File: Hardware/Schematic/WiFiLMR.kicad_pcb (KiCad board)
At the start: 2 copper layers, 8 parts, among them J1 Conn_01x03_Male, J2 Conn_01x02_Male, J3 Conn_01x04_Male, U1 ESP32-WROOM-32U

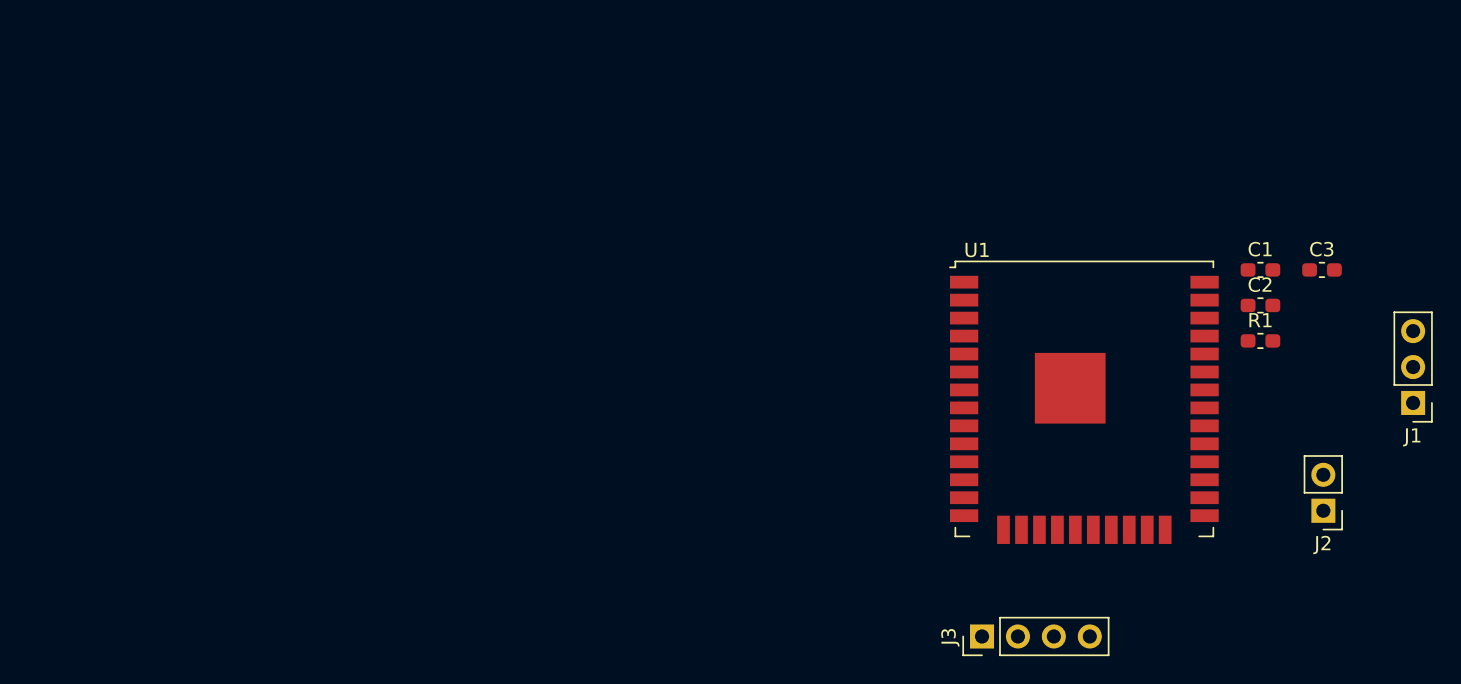
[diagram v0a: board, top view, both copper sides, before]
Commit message: Particle Photon Schematic Update
Added Particle Photon symbol, footprint & 3D model along with datasheet. Updated schematic with sockets to plugin a Photon board and a JTAG connector based off of the design in the Photon datasheet.
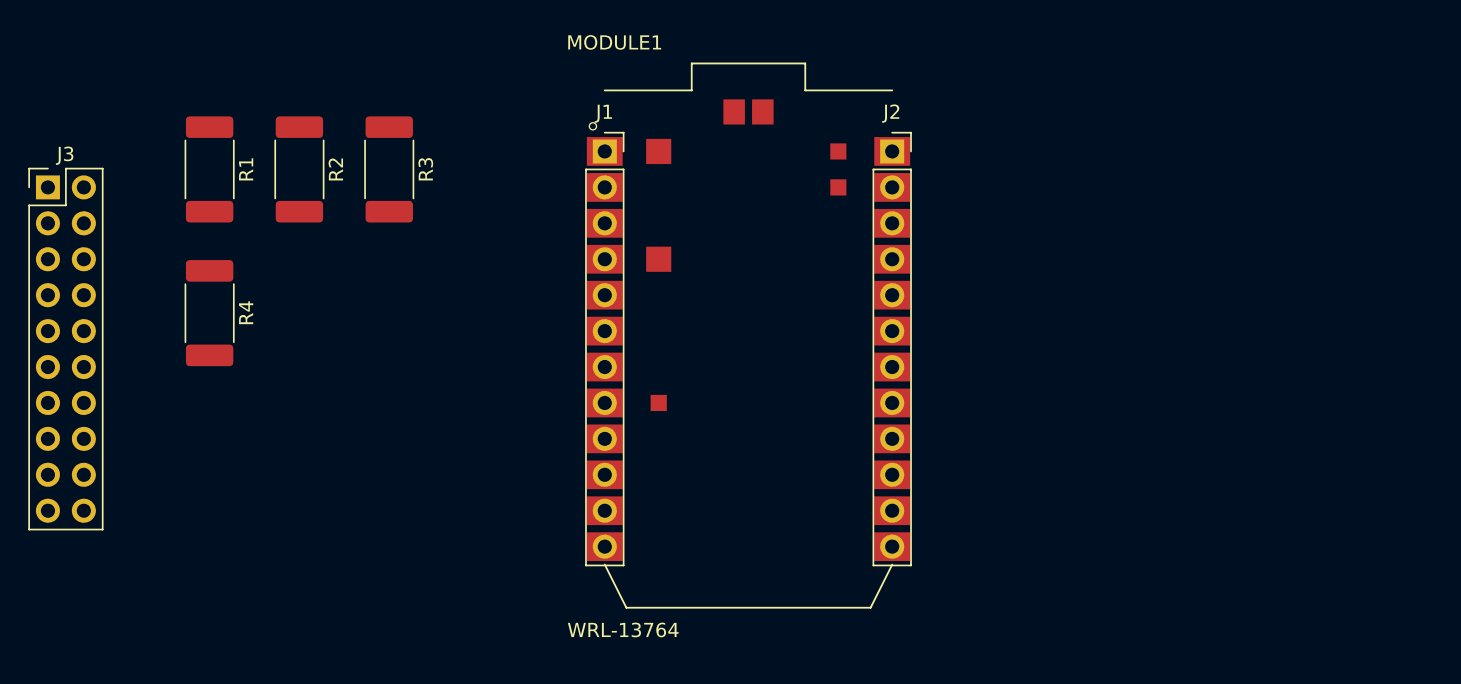
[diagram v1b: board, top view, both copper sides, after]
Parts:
- removed C1, C2, C3: 0.1uF, Capacitor_SMD:C_0603_1608Metric_Pad1.05x0.95mm_HandSolder
- removed U1: ESP32-WROOM-32U, RF_Module:ESP32-WROOM-32U
- added MODULE1: WRL-13764, WRL-13764:SPARKFUN_WRL-13764, F.Cu at (138.4, 91.4)
- added R2: R_Small_US, Resistor_SMD:R_2512_6332Metric_Pad1.52x3.35mm_HandSolder, F.Cu at (106.7, 78.7)
- added R3: R_Small_US, Resistor_SMD:R_2512_6332Metric_Pad1.52x3.35mm_HandSolder, F.Cu at (113.0, 78.7)
- added R4: R_Small_US, Resistor_SMD:R_2512_6332Metric_Pad1.52x3.35mm_HandSolder, F.Cu at (100.3, 88.9)
- J1: value Conn_01x03_Male -> Conn_01x12; footprint Connector_PinHeader_2.54mm:PinHeader_1x03_P2.54mm_Vertical -> Connector_PinSocket_2.54mm:PinSocket_1x12_P2.54mm_Vertical
- J2: value Conn_01x02_Male -> Conn_01x12; footprint Connector_PinHeader_2.54mm:PinHeader_1x02_P2.54mm_Vertical -> Connector_PinSocket_2.54mm:PinSocket_1x12_P2.54mm_Vertical
- J3: value Conn_01x04_Male -> JTAG; footprint Connector_PinHeader_2.54mm:PinHeader_1x04_P2.54mm_Vertical -> Connector_PinHeader_2.54mm:PinHeader_2x10_P2.54mm_Vertical
- R1: value 10K -> R_Small_US; footprint Resistor_SMD:R_0603_1608Metric_Pad1.05x0.95mm_HandSolder -> Resistor_SMD:R_2512_6332Metric_Pad1.52x3.35mm_HandSolder
- moved R1 75.3 mm to (100.3, 78.7), turned to 270 degrees
- moved J3 73.3 mm to (88.9, 80.0), turned to 0 degrees
- moved J1 59.9 mm to (128.3, 77.5), turned to 0 degrees
- moved J2 39.7 mm to (148.6, 77.5), turned to 0 degrees
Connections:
- J1 pad 1: Earth -> Net-(J1-Pad1)
- J1 pad 2: Net-(J1-Pad2) -> Earth
- J2 pad 2: Earth -> Net-(J2-Pad2)
- J3 pad 1: Net-(J3-Pad1) -> +3V3
- J3 pad 3: Net-(J3-Pad3) -> /TRST
- J3 pad 4: Net-(J3-Pad4) -> Earth
- R1 pad 2: Net-(C1-Pad2) -> /TRST

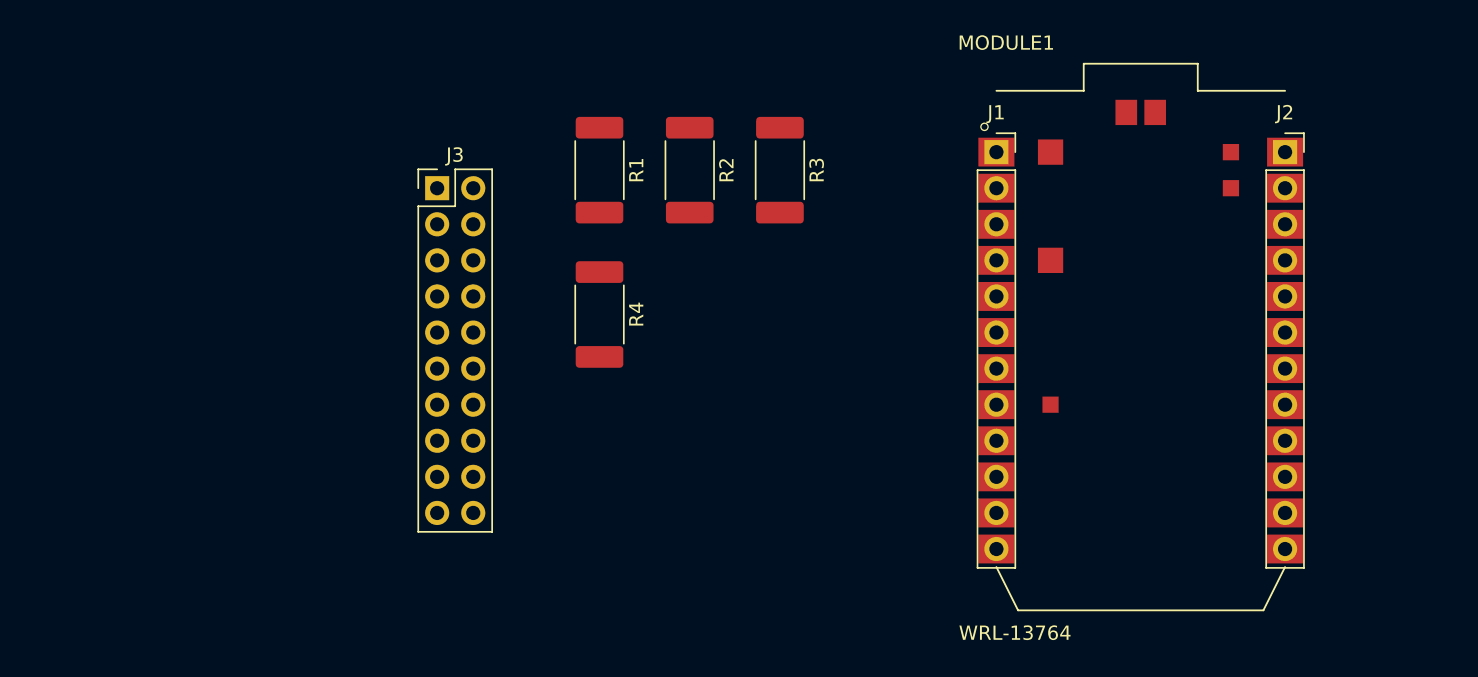
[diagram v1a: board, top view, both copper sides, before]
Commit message: Update schematic with JTAG and debug headers
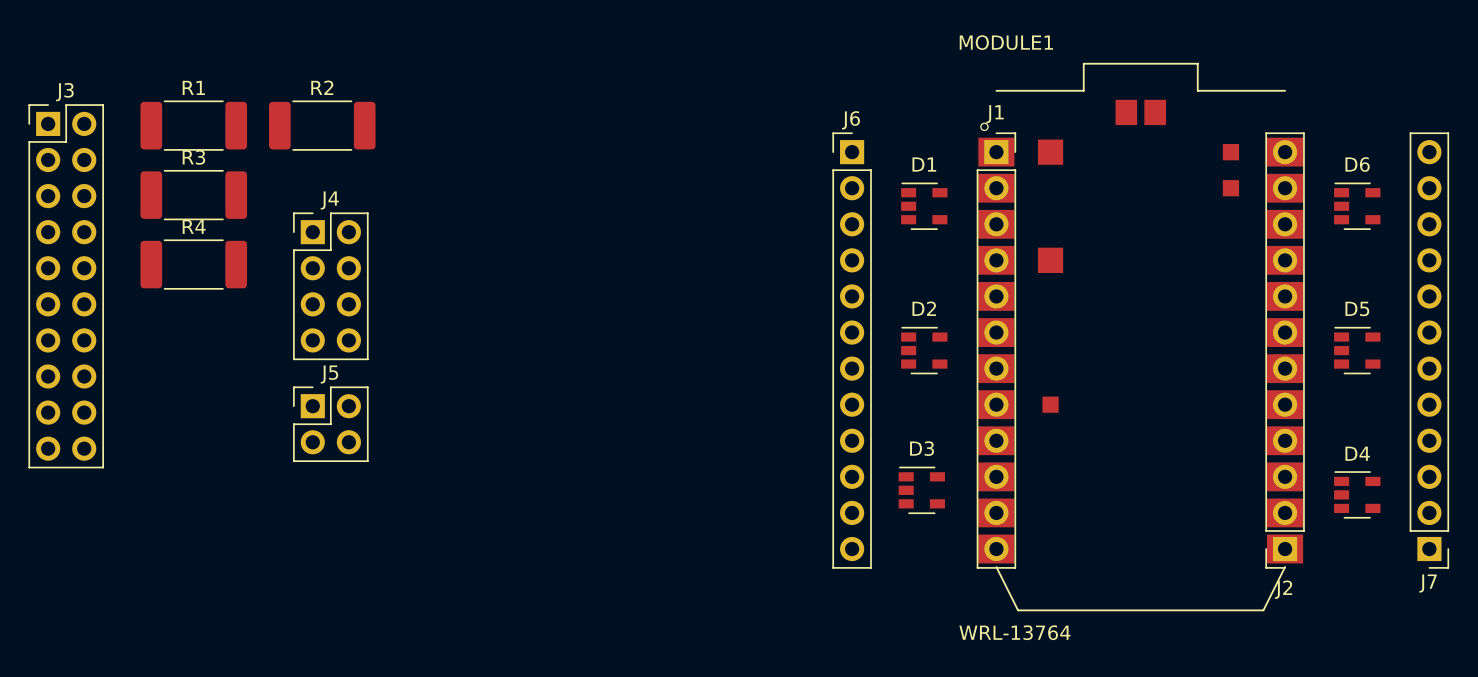
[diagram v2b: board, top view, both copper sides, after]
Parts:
- added D1: SP0504BAHT, Package_TO_SOT_SMD:SOT-23-5, F.Cu at (123.2, 81.3)
- added D2: SP0504BAHT, Package_TO_SOT_SMD:SOT-23-5, F.Cu at (123.2, 91.4)
- added D3: SP0504BAHT, Package_TO_SOT_SMD:SOT-23-5, F.Cu at (123.0, 101.3)
- added D4: SP0504BAHT, Package_TO_SOT_SMD:SOT-23-5, F.Cu at (153.7, 101.6)
- added D5: SP0504BAHT, Package_TO_SOT_SMD:SOT-23-5, F.Cu at (153.7, 91.4)
- added D6: SP0504BAHT, Package_TO_SOT_SMD:SOT-23-5, F.Cu at (153.7, 81.3)
- added J4: Conn_02x04_Odd_Even, Connector_PinHeader_2.54mm:PinHeader_2x04_P2.54mm_Vertical, F.Cu at (80.1, 83.1)
- added J5: Conn_02x02_Odd_Even, Connector_PinHeader_2.54mm:PinHeader_2x02_P2.54mm_Vertical, F.Cu at (80.1, 95.4)
- added J6: Conn_01x12, Connector_PinHeader_2.54mm:PinHeader_1x12_P2.54mm_Vertical, F.Cu at (118.1, 77.5)
- added J7: Conn_01x12, Connector_PinHeader_2.54mm:PinHeader_1x12_P2.54mm_Vertical, F.Cu at (158.8, 105.4)
- moved R3 41.3 mm to (71.8, 80.5), turned to 0 degrees
- moved R4 28.8 mm to (71.8, 85.4), turned to 0 degrees
- moved R1 28.7 mm to (71.8, 75.6), turned to 0 degrees
- moved J2 27.9 mm to (148.6, 105.4), turned to 180 degrees
- moved J3 27.8 mm to (61.5, 75.5)
- moved R2 26.1 mm to (80.8, 75.6), turned to 0 degrees
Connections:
- net Net-(J2-Pad10) renamed +BATT
- J1 pad 10: Net-(J1-Pad10) -> /Particle_Connector/ADC12|SPI_SS
- J1 pad 11: Net-(J1-Pad11) -> /Particle_Connector/ADC13
- J1 pad 12: Net-(J1-Pad12) -> /Particle_Connector/ADC15
- J1 pad 3: Net-(J1-Pad3) -> /Particle_Connector/USART1_TX|TIM1_CH2
- J1 pad 4: Net-(J1-Pad4) -> /Particle_Connector/USART1_RX|TIM1_CH3
- J1 pad 5: Net-(J1-Pad5) -> /Particle_Connector/WKUP|ADC0|TIM5_CH1
- J1 pad 6: Net-(J1-Pad6) -> /Particle_Connector/ADC4|DAC1
- J1 pad 7: Net-(J1-Pad7) -> /Particle_Connector/ADC7|SPI_MOSI|TIM3_CH2
- J1 pad 8: Net-(J1-Pad8) -> /Particle_Connector/ADC6|SPI_MISO|TIM3_CH1
- J1 pad 9: Net-(J1-Pad9) -> /Particle_Connector/ADC5|SPI_SCK|DAC2
- J2 pad 1: Net-(J2-Pad1) -> /Particle_Connector/SDA|TIM4_CH2
- J2 pad 11: /JTAG_RESET -> /Particle_Connector/RST
- J2 pad 2: Net-(J2-Pad2) -> /Particle_Connector/SCL|CAN2_TX|TIM4_CH1
- J2 pad 3: Net-(J2-Pad3) -> /Particle_Connector/SPI1_MOSI|CAN2_RX|TIM3_CH2|I2S3_SD
- J2 pad 4: /TRST -> /Particle_Connector/JTAG_TRST|SPI1_MISO|TIM3_CH1
- J2 pad 5: /TDO -> /Particle_Connector/JTAG_TDO|SPI1_SCK|I2S3_SCK
- J2 pad 6: /TDI -> /Particle_Connector/JTAG_TDI|SPI1_SS|I2S3_WS
- J2 pad 7: /TCK -> /Particle_Connector/JTAG_TCK
- J2 pad 8: /TMS -> /Particle_Connector/JTAG_TMS
- J3 pad 13: /TDO -> Net-(J3-Pad13)
- J3 pad 15: /JTAG_RESET -> Net-(J3-Pad15)
- J3 pad 3: /TRST -> Net-(J3-Pad3)
- J3 pad 5: /TDI -> Net-(J3-Pad5)
- J3 pad 7: /TMS -> Net-(J3-Pad7)
- J3 pad 9: /TCK -> Net-(J3-Pad9)
- R1 pad 2: /TRST -> Net-(J3-Pad3)
- R2 pad 2: /TDI -> Net-(J3-Pad5)
- R3 pad 2: /TMS -> Net-(J3-Pad7)
- R4 pad 2: /TCK -> Net-(J3-Pad9)

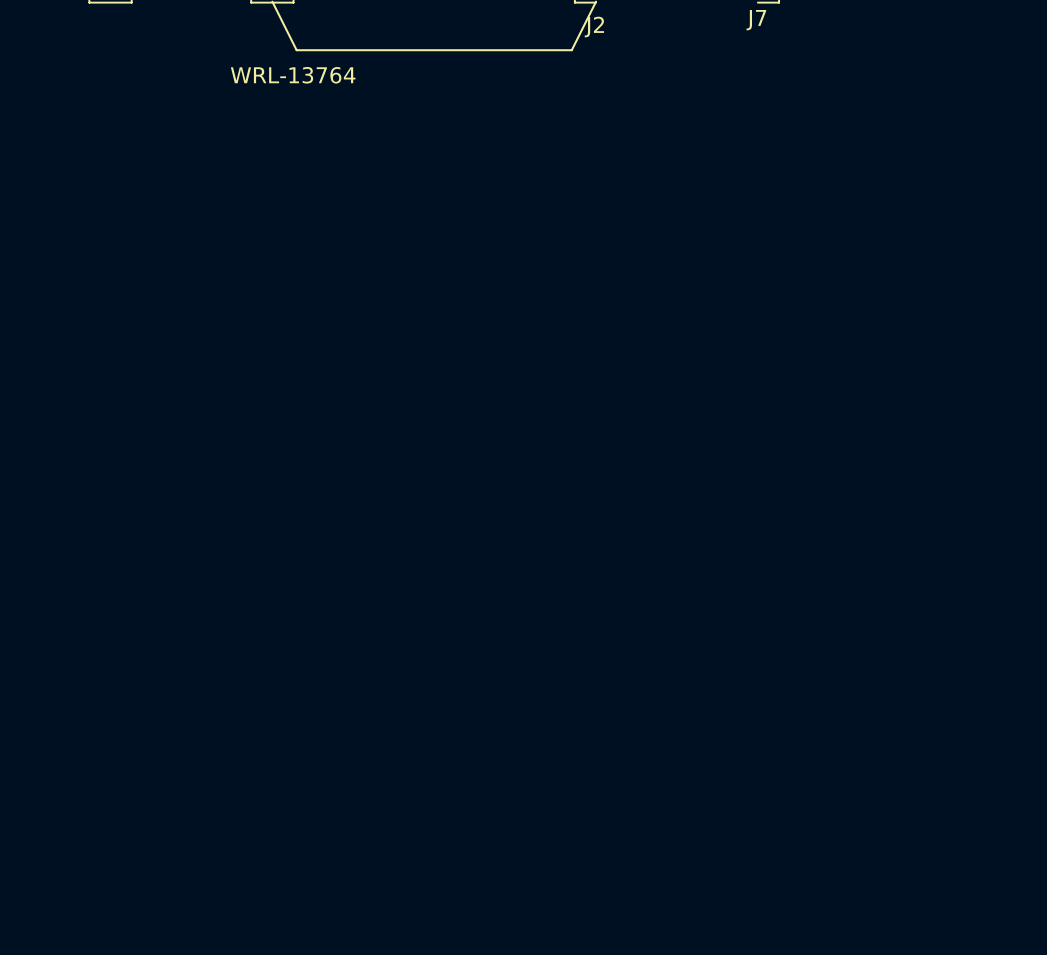
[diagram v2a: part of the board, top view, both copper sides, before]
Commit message: Added TCA8418 keyscan module to the schematic
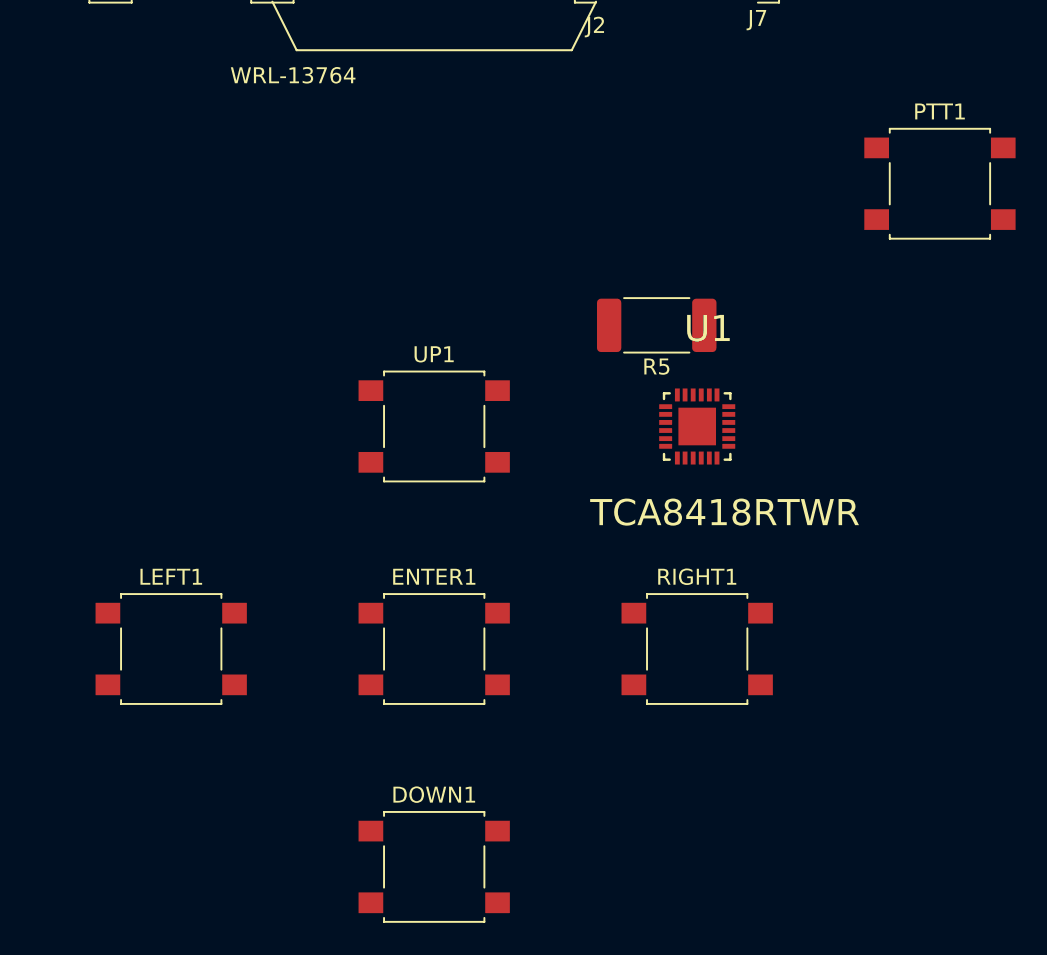
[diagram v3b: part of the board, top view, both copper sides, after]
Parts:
- added DOWN1: SW_Push, Button_Switch_SMD:SW_SPST_B3S-1000, F.Cu at (138.4, 161.0)
- added ENTER1: SW_Push, Button_Switch_SMD:SW_SPST_B3S-1000, F.Cu at (138.4, 147.3)
- added LEFT1: SW_Push, Button_Switch_SMD:SW_SPST_B3S-1000, F.Cu at (121.9, 147.3)
- added PTT1: SW_Push, Button_Switch_SMD:SW_SPST_B3S-1000, F.Cu at (170.2, 118.1)
- added R5: R_Small_US, Resistor_SMD:R_2512_6332Metric_Pad1.52x3.35mm_HandSolder, F.Cu at (152.4, 127.0)
- added RIGHT1: SW_Push, Button_Switch_SMD:SW_SPST_B3S-1000, F.Cu at (154.9, 147.3)
- added U1: TCA8418RTWR, TCA8418RTWR:QFN50P400X400X80-25N, F.Cu at (154.9, 133.3)
- added UP1: SW_Push, Button_Switch_SMD:SW_SPST_B3S-1000, F.Cu at (138.4, 133.3)
